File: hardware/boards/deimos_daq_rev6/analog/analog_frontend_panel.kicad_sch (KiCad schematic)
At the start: 13 parts, among them IC3001 BD42540FJ-CE2, IC3003 BD42540FJ-CE2, J3001 Screw_Terminal_01x12, J3002 Screw_Terminal_01x10, J3003 Screw_Terminal_01x12, J3004 Screw_Terminal_01x12, J3005 Screw_Terminal_01x10, J3006 Screw_Terminal_01x12

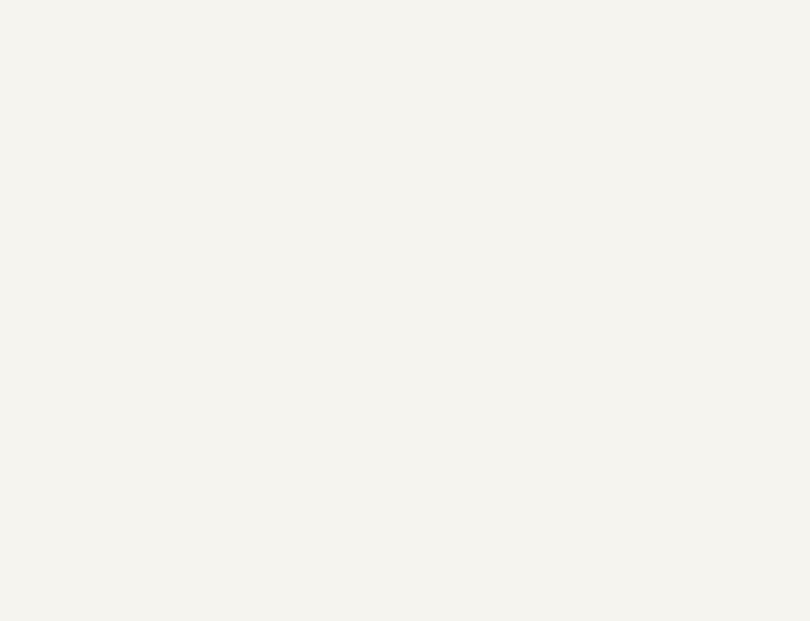
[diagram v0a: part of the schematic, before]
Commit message: move ovp diodes behind filter amps. wip to implement 5V LDO.
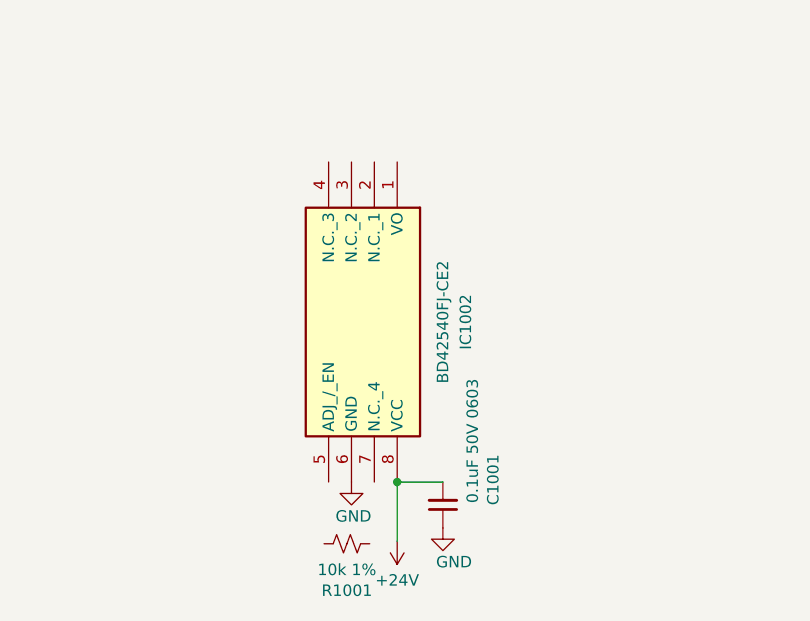
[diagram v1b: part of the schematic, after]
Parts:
- added C1001: 0.1uF 50V 0603, Capacitor_SMD:C_0603_1608Metric, symbol Device:C_Small
- added IC1002: BD42540FJ-CE2, aaa:SOIC127P600X175-8N, symbol aaa:BD42540FJ-CE2
- added R1001: 10k 1%, Resistor_SMD:R_0402_1005Metric, symbol Device:R_Small_US
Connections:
- net GND: now also C1001.1, IC1002.6 (GND)
- new net +24V: C1001.2, IC1002.8 (VCC)

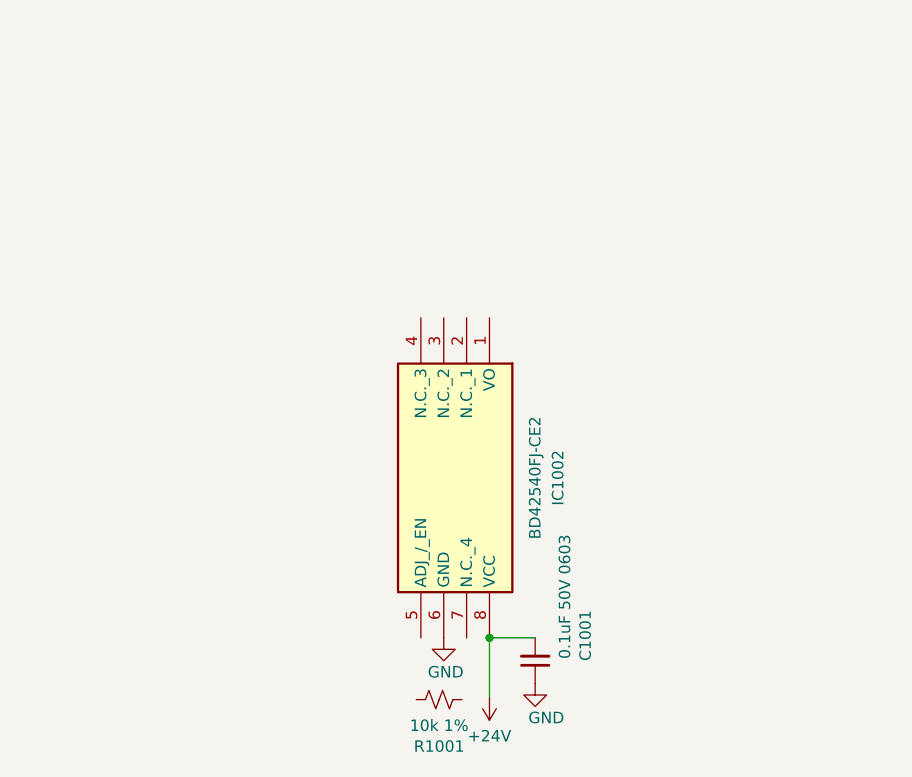
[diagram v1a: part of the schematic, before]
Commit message: figure out divider for 5V LDO. update input filter for resistance amp to cause less error.
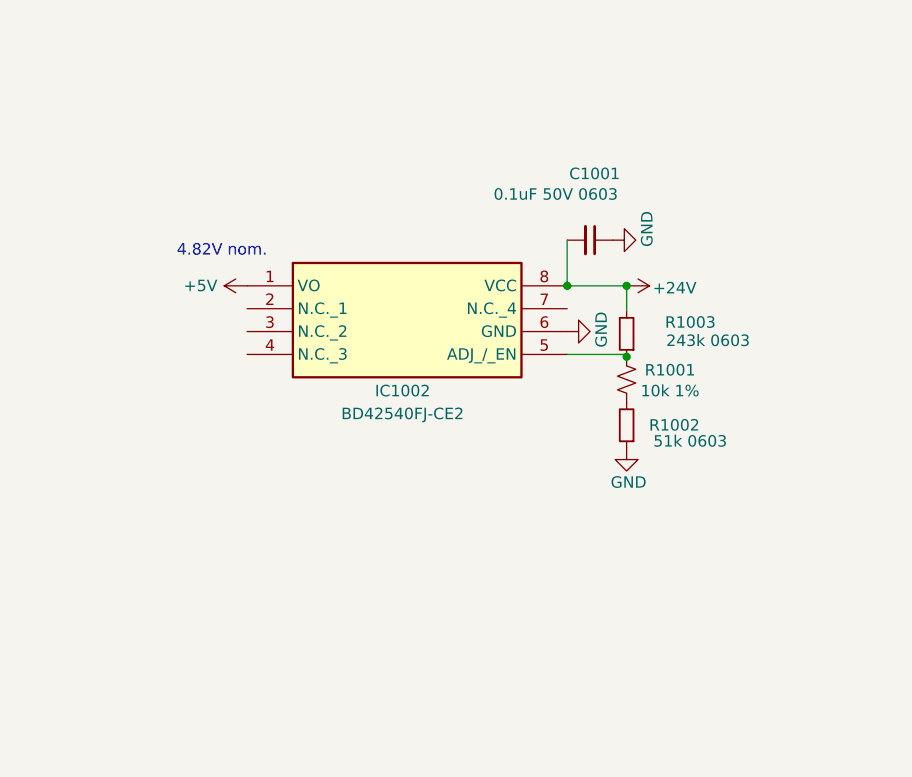
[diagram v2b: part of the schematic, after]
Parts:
- added R1002: 51k 0603, Resistor_SMD:R_0603_1608Metric, symbol Device:R_Small
- added R1003: 243k 0603, Resistor_SMD:R_0603_1608Metric, symbol Device:R_Small
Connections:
- net +24V: now also R1003.2
- net GND: now also R1002.1
- net at R1001.1: now also IC1002.5 (ADJ_/_EN), R1003.1
- net at R1001.2: now also R1002.2
- net +5V: now reaches IC1002.1 (VO)
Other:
- note added: "4.82V nom."
- moved on the sheet: C1001, IC1002, R1001

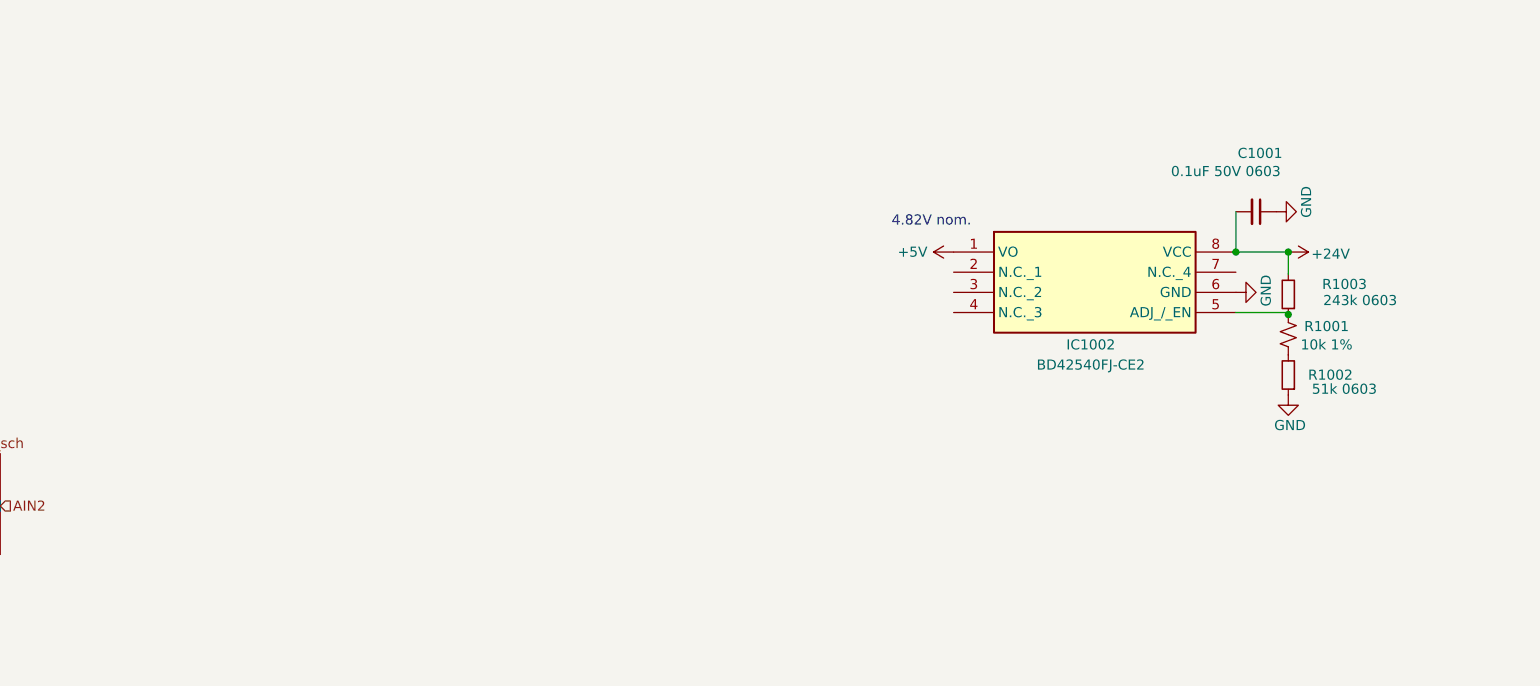
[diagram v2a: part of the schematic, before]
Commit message: label 5v ldo
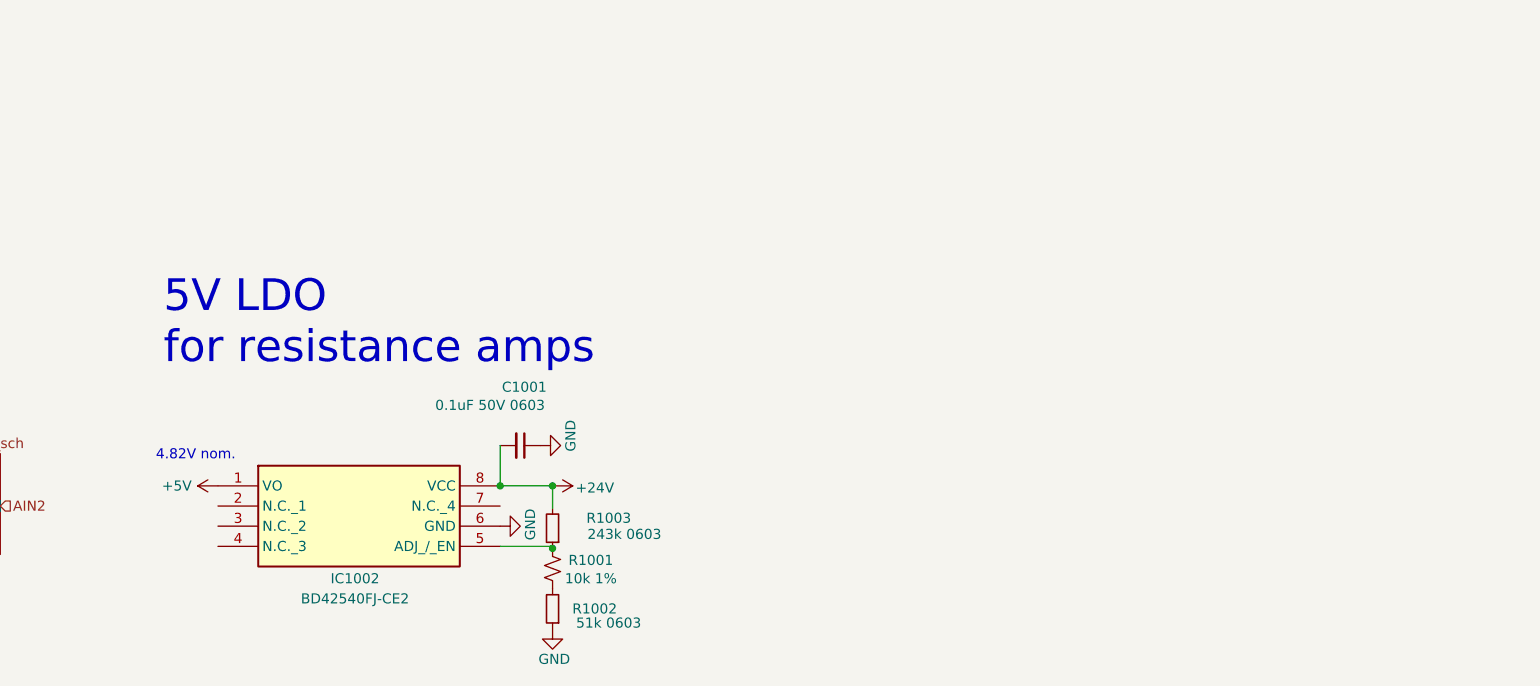
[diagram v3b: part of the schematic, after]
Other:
- note added: "5V LDO for resistance amps"
- moved on the sheet: C1001, IC1002, R1001, R1002, R1003

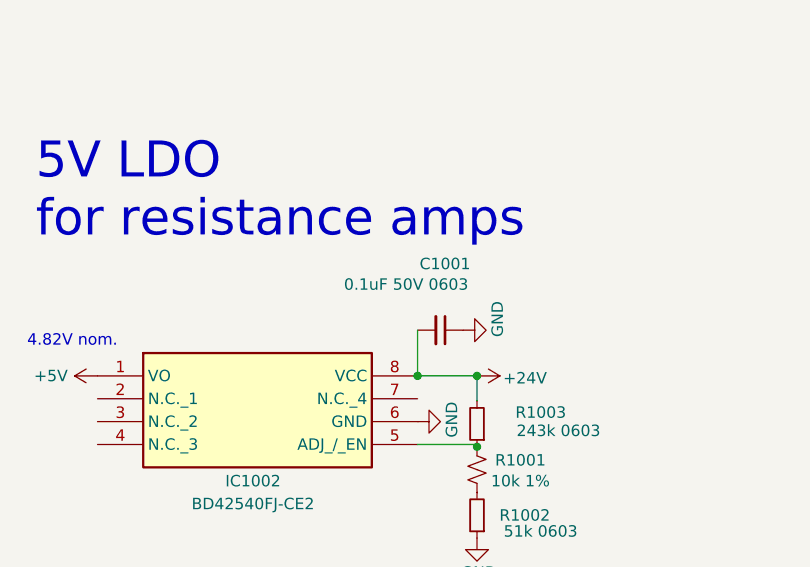
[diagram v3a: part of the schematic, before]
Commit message: run rtd amp current sinks on 5V supply
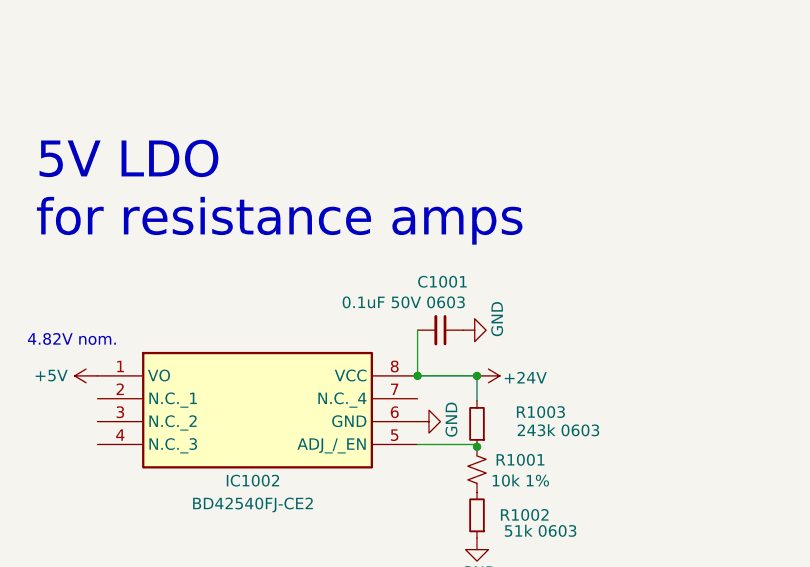
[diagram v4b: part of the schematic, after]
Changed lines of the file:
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@@
 		(dnp no)
 		(property "Reference" "C1001"
-			(at 144.78 247.904 90)
+			(at 144.526 249.936 90)
 			(effects
 				(font
@@
 		)
 		(property "Value" "0.1uF 50V 0603"
-			(at 140.462 250.19 90)
+			(at 140.208 252.222 90)
 			(effects
 				(font

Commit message: exclude testpoints from BOM
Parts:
- renumbered C1003 to C3001, C1002 to C3002, C1001 to C3003, IC1002 to IC3002, R1003 to R3002, R1001 to R3003, R1002 to R3004
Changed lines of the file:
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@@
 		(on_board yes)
 		(dnp no)
-		(property "Reference" "C1003"
+		(property "Reference" "C3001"
 			(at 47.498 127.762 90)
 			(effects
@@
 		)
 		(instances
+			(project "analog_i"
+				(path "/5a60c4b1-b6cb-416e-8883-8291fa089b87/c2baf18d-2b19-4edb-98b3-535275ee271f"
+					(reference "C3001")
+					(unit 1)
+				)
+			)
 			(project "analog_frontend_panel"
 				(path "/c241d083-1323-4b4a-a540-956d0afb7b72"
@@
 		(on_board yes)
 		(dnp no)
-		(property "Reference" "#PWR1002"
+		(property "Reference" "#PWR112"
 			(at 144.526 260.35 0)
 			(effects
@@
 		)
 		(instances
+			(project "analog_i"
+				(path "/5a60c4b1-b6cb-416e-8883-8291fa089b87/c2baf18d-2b19-4edb-98b3-535275ee271f"
+					(reference "#PWR112")
+					(unit 1)
+				)
+			)
 			(project ""
 				(path "/c241d083-1323-4b4a-a540-956d0afb7b72"
@@
 		(on_board yes)
 		(dnp no)
-		(property "Reference" "R1003"
+		(property "Reference" "R3002"
 			(at 158.242 264.414 0)
 			(effects
@@
 		)
 		(instances
+			(project "analog_i"
+				(path "/5a60c4b1-b6cb-416e-8883-8291fa089b87/c2baf18d-2b19-4edb-98b3-535275ee271f"
+					(reference "R3002")
+					(unit 1)
+				)
+			)
 			(project "analog_frontend_panel"
 				(path "/c241d083-1323-4b4a-a540-956d0afb7b72"
@@
 		(on_board yes)
 		(dnp no)
-		(property "Reference" "#PWR1024"
+		(property "Reference" "#PWR126"
 			(at 29.21 124.206 0)
 			(effects
@@
 		)
 		(instances
+			(project "analog_i"
+				(path "/5a60c4b1-b6cb-416e-8883-8291fa089b87/c2baf18d-2b19-4edb-98b3-535275ee271f"
+					(reference "#PWR126")
+					(unit 1)
+				)
+			)
 			(project "analog_frontend_panel"
 				(path "/c241d083-1323-4b4a-a540-956d0afb7b72"
@@
 		(on_board yes)
 		(dnp no)
-		(property "Reference" "#PWR1006"
+		(property "Reference" "#PWR102"
 			(at 148.336 284.734 0)
 			(effects
@@
 		)
 		(instances
+			(project "analog_i"
+				(path "/5a60c4b1-b6cb-416e-8883-8291fa089b87/c2baf18d-2b19-4edb-98b3-535275ee271f"
+					(reference "#PWR102")
+					(unit 1)
+				)
+			)
 			(project "analog_frontend_panel"
 				(path "/c241d083-1323-4b4a-a540-956d0afb7b72"
@@
 		(on_board yes)
 		(dnp no)
-		(property "Reference" "R1001"
+		(property "Reference" "R3003"
 			(at 153.162 269.7226 0)
 			(effects
@@
 		)
 		(instances
+			(project "analog_i"
+				(path "/5a60c4b1-b6cb-416e-8883-8291fa089b87/c2baf18d-2b19-4edb-98b3-535275ee271f"
+					(reference "R3003")
+					(unit 1)
+				)
+			)
 			(project "analog_frontend_panel"
 				(path "/c241d083-1323-4b4a-a540-956d0afb7b72"
@@
 		(on_board yes)
 		(dnp no)
-		(property "Reference" "#PWR1004"
+		(property "Reference" "#PWR113"
 			(at 148.082 265.43 0)
 			(effects
@@
 		)
 		(instances
+			(project "analog_i"
+				(path "/5a60c4b1-b6cb-416e-8883-8291fa089b87/c2baf18d-2b19-4edb-98b3-535275ee271f"
+					(reference "#PWR113")
+					(unit 1)
+				)
+			)
 			(project "analog_frontend_panel"
 				(path "/c241d083-1323-4b4a-a540-956d0afb7b72"
@@
 		(on_board yes)
 		(dnp no)
-		(property "Reference" "R1002"
+		(property "Reference" "R3004"
 			(at 156.464 275.844 0)
 			(effects
@@
 		)
 		(instances
+			(project "analog_i"
+				(path "/5a60c4b1-b6cb-416e-8883-8291fa089b87/c2baf18d-2b19-4edb-98b3-535275ee271f"
+					(reference "R3004")
+					(unit 1)
+				)
+			)
 			(project "analog_frontend_panel"
 				(path "/c241d083-1323-4b4a-a540-956d0afb7b72"
@@
 		(dnp no)
 		(fields_autoplaced yes)
-		(property "Reference" "#PWR1025"
+		(property "Reference" "#PWR103"
 			(at 109.982 260.35 0)
 			(effects
@@
 		)
 		(instances
+			(project "analog_i"
+				(path "/5a60c4b1-b6cb-416e-8883-8291fa089b87/c2baf18d-2b19-4edb-98b3-535275ee271f"
+					(reference "#PWR103")
+					(unit 1)
+				)
+			)
 			(project ""
 				(path "/c241d083-1323-4b4a-a540-956d0afb7b72"
@@
 		(on_board yes)
 		(dnp no)
-		(property "Reference" "#PWR1023"
+		(property "Reference" "#PWR131"
 			(at 56.642 123.444 0)
 			(effects
@@
 		)
 		(instances
+			(project "analog_i"
+				(path "/5a60c4b1-b6cb-416e-8883-8291fa089b87/c2baf18d-2b19-4edb-98b3-535275ee271f"
+					(reference "#PWR131")
+					(unit 1)
+				)
+			)
 			(project "analog_frontend_panel"
 				(path "/c241d083-1323-4b4a-a540-956d0afb7b72"
@@
 		(on_board yes)
 		(dnp no)
-		(property "Reference" "#PWR1018"
+		(property "Reference" "#PWR125"
 			(at 36.83 124.206 0)
 			(effects
@@
 		)
 		(instances
+			(project "analog_i"
+				(path "/5a60c4b1-b6cb-416e-8883-8291fa089b87/c2baf18d-2b19-4edb-98b3-535275ee271f"
+					(reference "#PWR125")
+					(unit 1)
+				)
+			)
 			(project ""
 				(path "/c241d083-1323-4b4a-a540-956d0afb7b72"
@@
 		(on_board yes)
 		(dnp no)
-		(property "Reference" "#PWR1017"
+		(property "Reference" "#PWR132"
 			(at 69.342 138.684 0)
 			(effects
@@
 		)
 		(instances
+			(project "analog_i"
+				(path "/5a60c4b1-b6cb-416e-8883-8291fa089b87/c2baf18d-2b19-4edb-98b3-535275ee271f"
+					(reference "#PWR132")
+					(unit 1)
+				)
+			)
 			(project "analog_frontend_panel"
 				(path "/c241d083-1323-4b4a-a540-956d0afb7b72"
@@
 		(on_board yes)
 		(dnp no)
-		(property "Reference" "IC1002"
+		(property "Reference" "IC3002"
 			(at 123.444 272.034 0)
 			(effects
@@
 		)
 		(instances
+			(project "analog_i"
+				(path "/5a60c4b1-b6cb-416e-8883-8291fa089b87/c2baf18d-2b19-4edb-98b3-535275ee271f"
+					(reference "IC3002")
+					(unit 1)
+				)
+			)
 			(project "analog_frontend_panel"
 				(path "/c241d083-1323-4b4a-a540-956d0afb7b72"
@@
 		(on_board yes)
 		(dnp no)
-		(property "Reference" "C1002"
+		(property "Reference" "C3002"
 			(at 74.93 127 90)
 			(effects
@@
 		)
 		(instances
+			(project "analog_i"
+				(path "/5a60c4b1-b6cb-416e-8883-8291fa089b87/c2baf18d-2b19-4edb-98b3-535275ee271f"
+					(reference "C3002")
+					(unit 1)
+				)
+			)
 			(project "analog_frontend_panel"
 				(path "/c241d083-1323-4b4a-a540-956d0afb7b72"
@@
 		(on_board yes)
 		(dnp no)
-		(property "Reference" "C1001"
+		(property "Reference" "C3003"
 			(at 144.526 249.936 90)
 			(effects
@@
 		)
 		(instances
+			(project "analog_i"
+				(path "/5a60c4b1-b6cb-416e-8883-8291fa089b87/c2baf18d-2b19-4edb-98b3-535275ee271f"
+					(reference "C3003")
+					(unit 1)
+				)
+			)
 			(project "analog_frontend_panel"
 				(path "/c241d083-1323-4b4a-a540-956d0afb7b72"
@@
 		(on_board yes)
 		(dnp no)
-		(property "Reference" "#PWR1020"
+		(property "Reference" "#PWR128"
 			(at 41.91 139.446 0)
 			(effects
@@
 		)
 		(instances
+			(project "analog_i"
+				(path "/5a60c4b1-b6cb-416e-8883-8291fa089b87/c2baf18d-2b19-4edb-98b3-535275ee271f"
+					(reference "#PWR128")
+					(unit 1)
+				)
+			)
 			(project "analog_frontend_panel"
 				(path "/c241d083-1323-4b4a-a540-956d0afb7b72"
@@
 		(on_board yes)
 		(dnp no)
-		(property "Reference" "#PWR1022"
+		(property "Reference" "#PWR114"
 			(at 153.162 255.27 0)
 			(effects
@@
 		)
 		(instances
+			(project "analog_i"
+				(path "/5a60c4b1-b6cb-416e-8883-8291fa089b87/c2baf18d-2b19-4edb-98b3-535275ee271f"
+					(reference "#PWR114")
+					(unit 1)
+				)
+			)
 			(project "analog_frontend_panel"
 				(path "/c241d083-1323-4b4a-a540-956d0afb7b72"
